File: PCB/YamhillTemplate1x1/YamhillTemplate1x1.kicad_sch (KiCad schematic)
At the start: 0 parts

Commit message: Fix PCB template problems
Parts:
- added H1, H2, H3, H4: MountingHole_Pad, MountingHole:MountingHole_3.2mm_M3_Pad_Via, symbol Mechanical:MountingHole_Pad
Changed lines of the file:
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@@
     (company "Etherkit")
+  )
+  (symbol (lib_id "Graphic:Logo_Open_Hardware_Small") (at 144.526 177.546 0) (unit 1)
+    (in_bom no) (on_board no) (dnp no) (fields_autoplaced)
+    (property "Reference" "#SYM1" (at 144.526 170.561 0)
+      (effects (font (size 1.27 1.27)) hide)
+    )
+    (property "Value" "Logo_Open_Hardware_Small" (at 144.526 183.261 0)
+      (effects (font (size 1.27 1.27)) hide)
+    )
+    (property "Footprint" "EtherkitKicadLibrary:OSHWLogo4mm" (at 144.526 177.546 0)
+      (effects (font (size 1.27 1.27)) hide)
+    )
+    (property "Datasheet" "~" (at 144.526 177.546 0)
+      (effects (font (size 1.27 1.27)) hide)
+    )
+    (property "Sim.Enable" "0" (at 144.526 177.546 0)
+      (effects (font (size 1.27 1.27)) hide)
+    )
+    (instances
+      (project "YamhillTemplate1x1"
+        (path "/49f62868-e637-46b0-b067-683e675fe4a7"
+          (reference "#SYM1") (unit 1)
+        )
+      )
+    )
+  )
+  (symbol (lib_id "Mechanical:MountingHole_Pad") (at 106.68 190.5 0) (unit 1)
+    (in_bom yes) (on_board yes) (dnp no)
+    (property "Reference" "H1" (at 109.982 188.595 0)
+      (effects (font (size 1.27 1.27)) (justify left))
+    )
+    (property "Value" "MountingHole_Pad" (at 109.982 191.135 0)
+      (effects (font (size 1.27 1.27)) (justify left))
+    )
+    (property "Footprint" "MountingHole:MountingHole_3.2mm_M3_Pad_Via" (at 106.68 190.5 0)
+      (effects (font (size 1.27 1.27)) hide)
+    )
+    (property "Datasheet" "~" (at 106.68 190.5 0)
+      (effects (font (size 1.27 1.27)) hide)
+    )
+    (pin "1")
+    (instances
+      (project "YamhillTemplate1x1"
+        (path "/49f62868-e637-46b0-b067-683e675fe4a7"
+          (reference "H1") (unit 1)
+        )
+      )
+    )
+  )
+  (symbol (lib_id "EtherkitKicadLibrary:LOGO") (at 119.126 176.53 0) (unit 1)
+    (in_bom yes) (on_board yes) (dnp no) (fields_autoplaced)
+    (property "Reference" "#G1" (at 119.126 172.165 0)
+      (effects (font (size 1.27 1.27)) hide)
+    )
+    (property "Value" "LOGO" (at 119.126 180.895 0)
+      (effects (font (size 1.27 1.27)) hide)
+    )
+    (property "Footprint" "EtherkitKicadLibrary:EtherkitLogoSmall" (at 119.126 176.53 0)
+      (effects (font (size 1.27 1.27)) hide)
+    )
+    (property "Datasheet" "" (at 119.126 176.53 0)
+      (effects (font (size 1.27 1.27)) hide)
+    )
+    (instances
+      (project "YamhillTemplate1x1"
+        (path "/49f62868-e637-46b0-b067-683e675fe4a7"
+          (reference "#G1") (unit 1)
+        )
+      )
+    )
+  )
+  (symbol (lib_id "Mechanical:MountingHole_Pad") (at 106.68 198.12 0) (unit 1)
+    (in_bom yes) (on_board yes) (dnp no) (fields_autoplaced)
+    (property "Reference" "H3" (at 110.236 196.215 0)
+      (effects (font (size 1.27 1.27)) (justify left))
+    )
+    (property "Value" "MountingHole_Pad" (at 110.236 198.755 0)
+      (effects (font (size 1.27 1.27)) (justify left))
+    )
+    (property "Footprint" "MountingHole:MountingHole_3.2mm_M3_Pad_Via" (at 106.68 198.12 0)
+      (effects (font (size 1.27 1.27)) hide)
+    )
+    (property "Datasheet" "~" (at 106.68 198.12 0)
+      (effects (font (size 1.27 1.27)) hide)
+    )
+    (pin "1")
+    (instances
+      (project "YamhillTemplate1x1"
+        (path "/49f62868-e637-46b0-b067-683e675fe4a7"
+          (reference "H3") (unit 1)
+        )
+      )
+    )
+  )
+  (symbol (lib_id "Mechanical:MountingHole_Pad") (at 131.826 197.866 0) (unit 1)
+    (in_bom yes) (on_board yes) (dnp no) (fields_autoplaced)
+    (property "Reference" "H4" (at 134.62 195.961 0)
+      (effects (font (size 1.27 1.27)) (justify left))
+    )
+    (property "Value" "MountingHole_Pad" (at 134.62 198.501 0)
+      (effects (font (size 1.27 1.27)) (justify left))
+    )
+    (property "Footprint" "MountingHole:MountingHole_3.2mm_M3_Pad_Via" (at 131.826 197.866 0)
+      (effects (font (size 1.27 1.27)) hide)
+    )
+    (property "Datasheet" "~" (at 131.826 197.866 0)
+      (effects (font (size 1.27 1.27)) hide)
+    )
+    (pin "1")
+    (instances
+      (project "YamhillTemplate1x1"
+        (path "/49f62868-e637-46b0-b067-683e675fe4a7"
+          (reference "H4") (unit 1)
+        )
+      )
+    )
+  )
+  (symbol (lib_id "Mechanical:MountingHole_Pad") (at 132.08 190.246 0) (unit 1)
+    (in_bom yes) (on_board yes) (dnp no) (fields_autoplaced)
+    (property "Reference" "H2" (at 134.874 188.341 0)
+      (effects (font (size 1.27 1.27)) (justify left))
+    )
+    (property "Value" "MountingHole_Pad" (at 134.874 190.881 0)
+      (effects (font (size 1.27 1.27)) (justify left))
+    )
+    (property "Footprint" "MountingHole:MountingHole_3.2mm_M3_Pad_Via" (at 132.08 190.246 0)
+      (effects (font (size 1.27 1.27)) hide)
+    )
+    (property "Datasheet" "~" (at 132.08 190.246 0)
+      (effects (font (size 1.27 1.27)) hide)
+    )
+    (pin "1")
+    (instances
+      (project "YamhillTemplate1x1"
+        (path "/49f62868-e637-46b0-b067-683e675fe4a7"
+          (reference "H2") (unit 1)
+        )
+      )
+    )
   )
   (sheet_instances

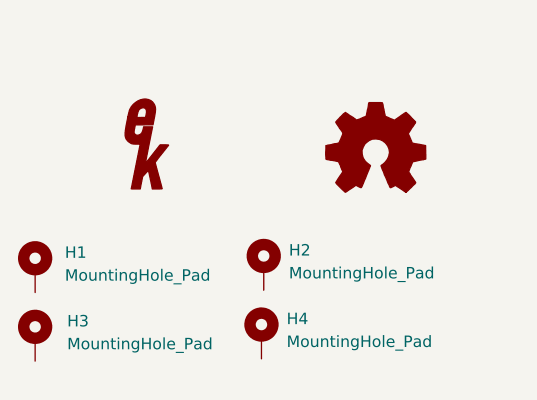
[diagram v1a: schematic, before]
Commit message: Add Diode Ring Mixer Board
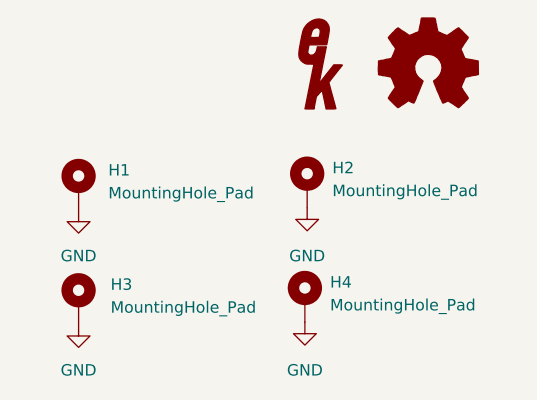
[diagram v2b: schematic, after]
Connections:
- net GND: now reaches H1.1
- net GND: now also H2.1, H3.1, H4.1
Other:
- moved on the sheet: H1, H2, H3, H4
